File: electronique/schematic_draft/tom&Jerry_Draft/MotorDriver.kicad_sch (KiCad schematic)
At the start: 9 parts, among them IC1401 NCS199A2RSQT2G, U1401 ZXBM5210-S

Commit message: STM32 KiCAD V5 - 20.09.2024
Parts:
- added D1401, D1402: RED, LED_SMD:LED_0603_1608Metric_Pad1.05x0.95mm_HandSolder, symbol Device:LED_Small
- added R1403, R1404: 390R, Resistor_SMD:R_0603_1608Metric_Pad0.98x0.95mm_HandSolder, symbol Device:R_Small
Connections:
- net GND: now also R1403.2, R1404.2
- net PWM_MOTx_CH1: now also D1401.2 (A)
- net PWM_MOTx_CH2: now also D1402.2 (A)
- new net: D1402.1 (K), R1404.1
- new net: D1401.1 (K), R1403.1
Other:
- note added: "Frequence du PWM de 10kHZ, pas sure que les LEDS tiennent la frequence"

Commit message: STM32 KiCAD V5 - 25.09.2024 - Ajout connecteurs TOF, ...
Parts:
- IC1401: footprint Library:SOT65P210X110-6N -> Package_TO_SOT_SMD:SC-70-8
- U1401: footprint Package_SO:SOIC-8-1EP_3.9x4.9mm_P1.27mm_EP2.62x3.51mm_ThermalVias -> Package_SO:Diodes_SO-8EP
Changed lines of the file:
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@@
 			)
 		)
-		(property "Footprint" "Package_SO:SOIC-8-1EP_3.9x4.9mm_P1.27mm_EP2.62x3.51mm_ThermalVias"
+		(property "Footprint" "Package_SO:Diodes_SO-8EP"
 			(at 119.38 107.95 0)
 			(effects
@@
 			)
 		)
-		(property "Footprint" "Library:SOT65P210X110-6N"
+		(property "Footprint" "Package_TO_SOT_SMD:SC-70-8"
 			(at 149.86 -11.1 0)
 			(effects

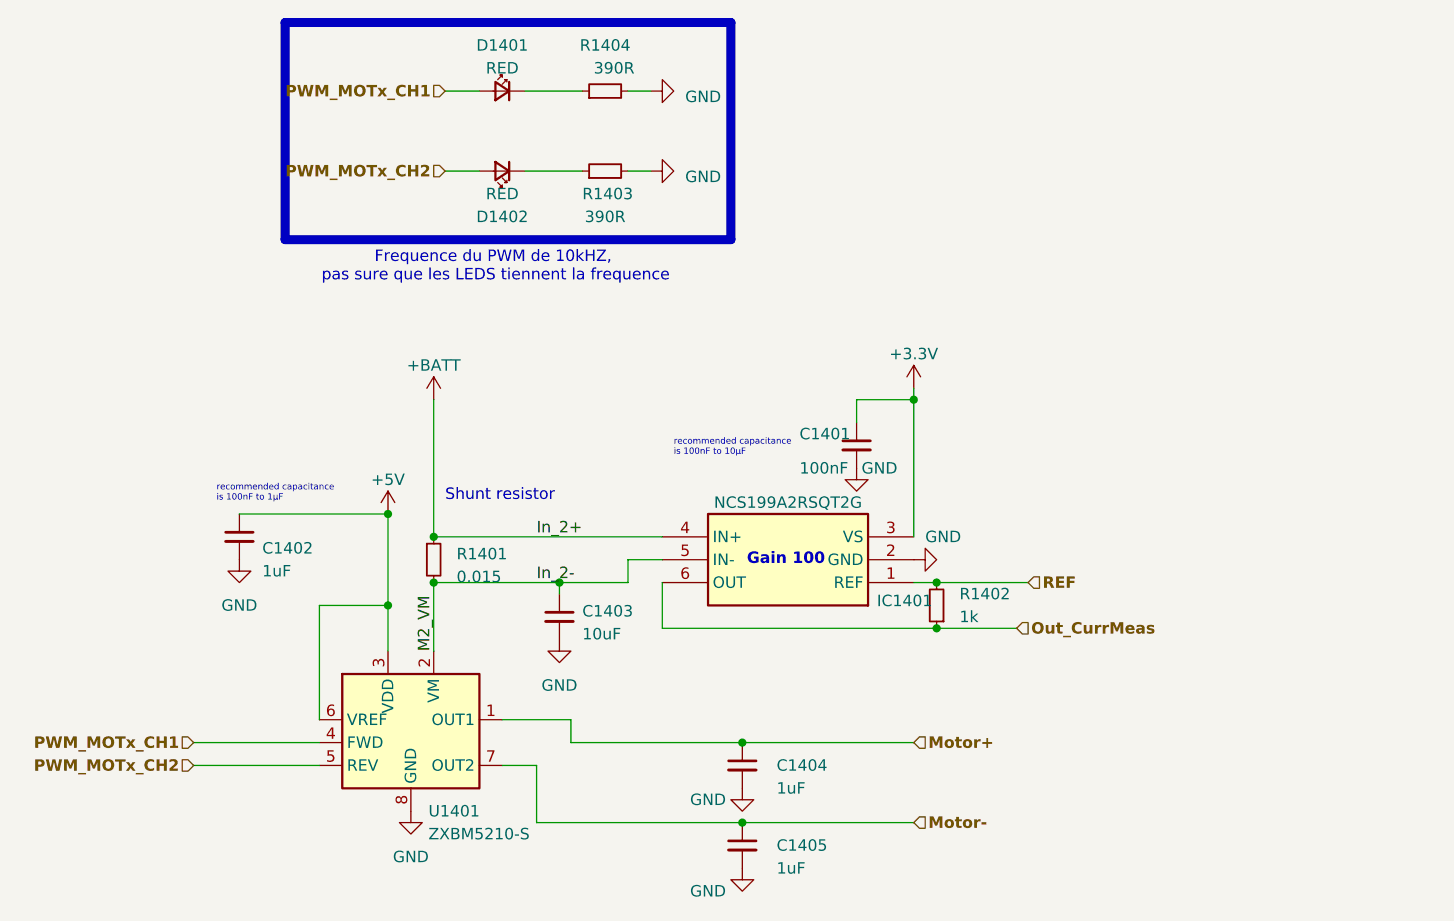
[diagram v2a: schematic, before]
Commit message: STM32 KiCAD v2.0 x CubeIDE - Pin definitif + schematic reviewed
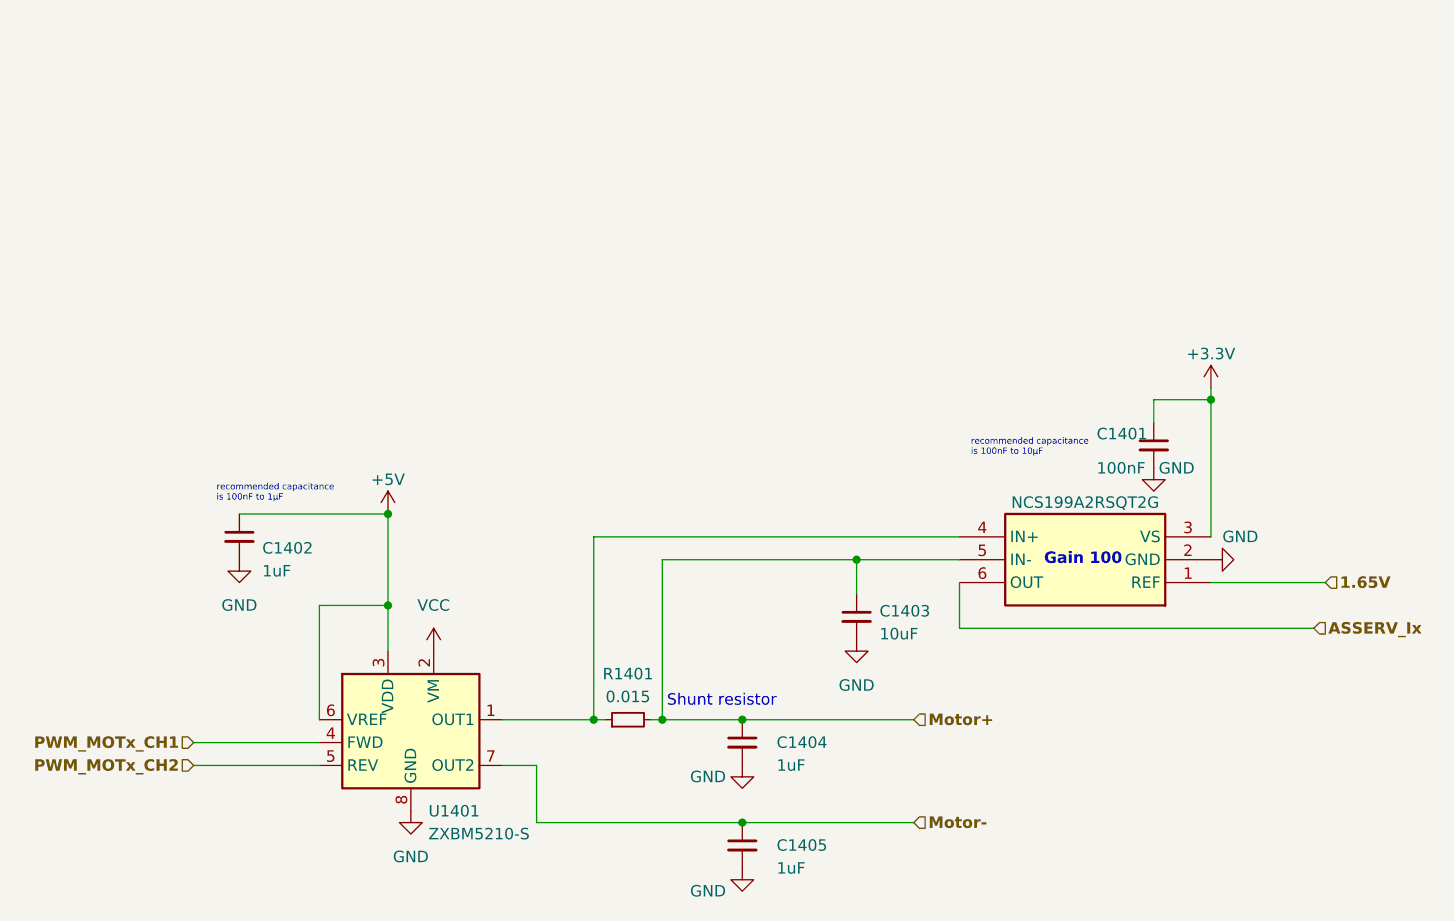
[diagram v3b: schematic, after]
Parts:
- removed D1401, D1402: RED, LED_SMD:LED_0603_1608Metric_Pad1.05x0.95mm_HandSolder, symbol Device:LED_Small
- removed R1402: 1k, symbol Device:R_Small
- removed R1403, R1404: 390R, Resistor_SMD:R_0603_1608Metric_Pad0.98x0.95mm_HandSolder, symbol Device:R_Small
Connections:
- net Motor+: now also C1403.1, IC1401.5 (IN-), R1401.2; no longer U1401.1 (OUT1)
- net +BATT: no longer names the net of IC1401.4 (IN+), R1401.1
- net +BATT: now also U1401.1 (OUT1)
- removed net In_2-: C1403.1, IC1401.5 (IN-), R1401.2, U1401.2 (VM)
- net Out_CurrMeas renamed ASSERV_Ix
- net REF renamed 1.65V
- new net VCC: U1401.2 (VM)
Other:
- note removed: "Frequence du PWM de 10kHZ, pas sure que les LEDS tiennent la frequence"
- moved on the sheet: C1401, C1403, C1404

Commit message: Adding footprint V0.1
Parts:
- C1401: footprint Capacitor_SMD:C_0603_1608Metric_Pad1.08x0.95mm_HandSolder -> Capacitor_SMD:C_0402_1005Metric
- C1402, C1403, C1404, C1405: footprint Capacitor_SMD:C_0603_1608Metric_Pad1.08x0.95mm_HandSolder -> Capacitor_SMD:C_0603_1608Metric
- IC1401: footprint Package_TO_SOT_SMD:SC-70-8 -> Tom&Jerry:SOT65P210X110-6N
- R1401: footprint Resistor_SMD:R_1206_3216Metric_Pad1.30x1.75mm_HandSolder -> Resistor_SMD:R_0402_1005Metric
- U1401: footprint Package_SO:Diodes_SO-8EP -> Tom&Jerry:SOIC127P600X175-8N
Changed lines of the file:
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@@
 			)
 		)
-		(property "Footprint" "Capacitor_SMD:C_0603_1608Metric_Pad1.08x0.95mm_HandSolder"
+		(property "Footprint" "Capacitor_SMD:C_0603_1608Metric"
 			(at 154.94 113.03 0)
 			(effects
@@
 			)
 		)
-		(property "Footprint" "Capacitor_SMD:C_0603_1608Metric_Pad1.08x0.95mm_HandSolder"
+		(property "Footprint" "Capacitor_SMD:C_0603_1608Metric"
 			(at 167.64 87.63 0)
 			(effects
@@
 			)
 		)
-		(property "Footprint" "Package_SO:Diodes_SO-8EP"
+		(property "Footprint" "Tom&Jerry:SOIC127P600X175-8N"
 			(at 119.38 107.95 0)
 			(effects
@@
 			)
 		)
-		(property "Footprint" "Resistor_SMD:R_1206_3216Metric_Pad1.30x1.75mm_HandSolder"
+		(property "Footprint" "Resistor_SMD:R_0402_1005Metric"
 			(at 142.24 99.06 0)
 			(effects
@@
 			)
 		)
-		(property "Footprint" "Capacitor_SMD:C_0603_1608Metric_Pad1.08x0.95mm_HandSolder"
+		(property "Footprint" "Capacitor_SMD:C_0603_1608Metric"
 			(at 99.06 78.74 0)
 			(effects
@@
 			)
 		)
-		(property "Footprint" "Capacitor_SMD:C_0603_1608Metric_Pad1.08x0.95mm_HandSolder"
+		(property "Footprint" "Capacitor_SMD:C_0603_1608Metric"
 			(at 154.94 101.6 0)
 			(effects
@@
 			)
 		)
-		(property "Footprint" "Package_TO_SOT_SMD:SC-70-8"
+		(property "Footprint" "Tom&Jerry:SOT65P210X110-6N"
 			(at 182.88 -11.1 0)
 			(effects
@@
 			)
 		)
-		(property "Footprint" "Capacitor_SMD:C_0603_1608Metric_Pad1.08x0.95mm_HandSolder"
+		(property "Footprint" "Capacitor_SMD:C_0402_1005Metric"
 			(at 200.66 68.58 0)
 			(effects

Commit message: Ajout des bonnes empreintes
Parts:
- U1401: footprint Tom&Jerry:SOIC127P600X175-8N -> Tom&Jerry:XBM5210
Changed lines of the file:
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@@
 			)
 		)
-		(property "Footprint" "Tom&Jerry:SOIC127P600X175-8N"
+		(property "Footprint" "Tom&Jerry:XBM5210"
 			(at 119.38 107.95 0)
 			(effects

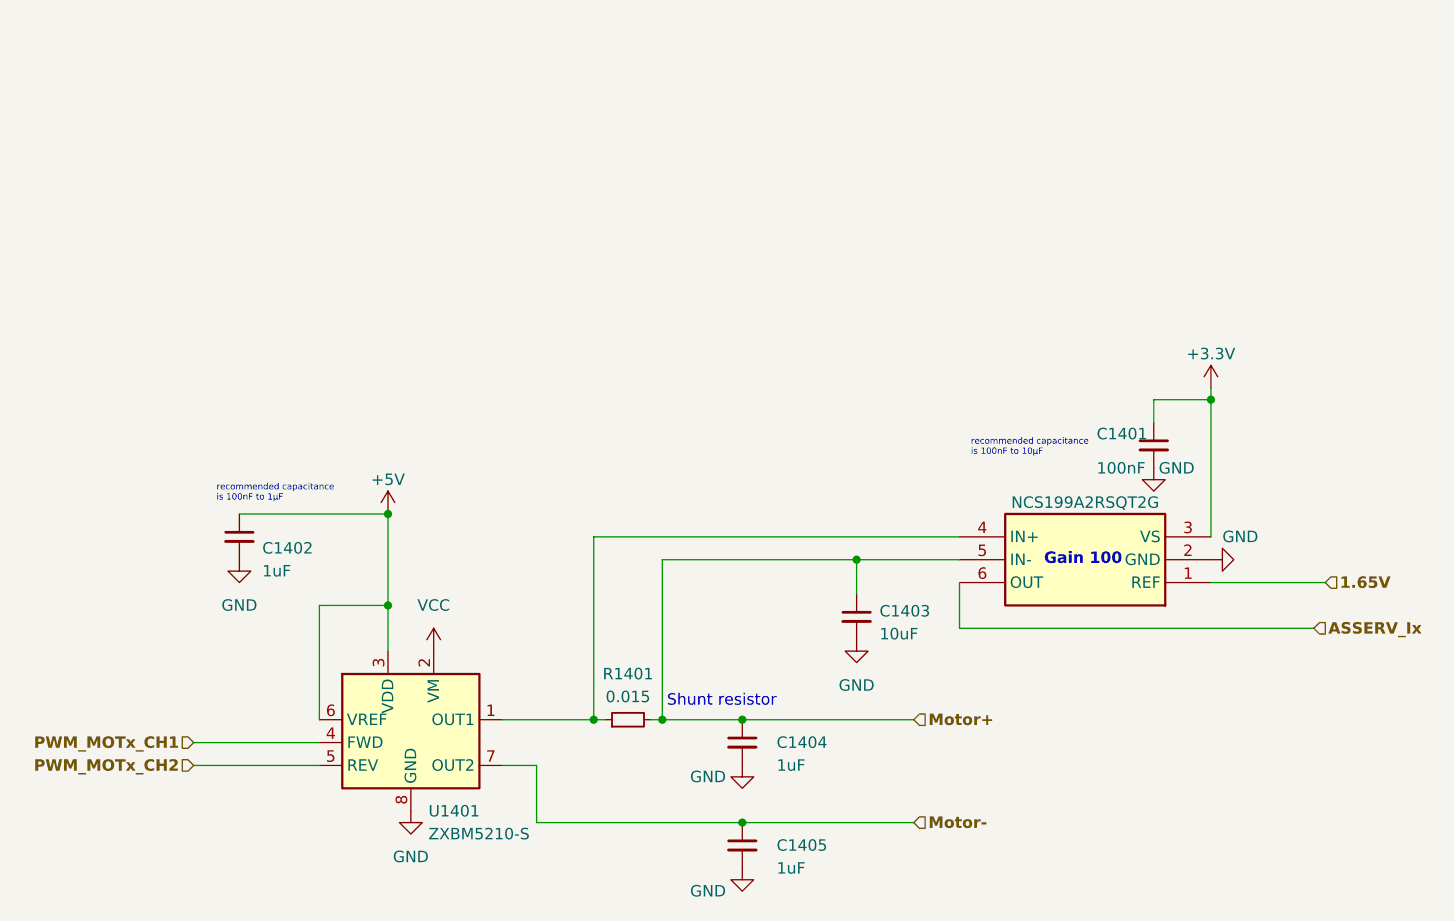
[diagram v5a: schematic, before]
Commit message: Ajout V2 TOF + MultiPCB Panalize
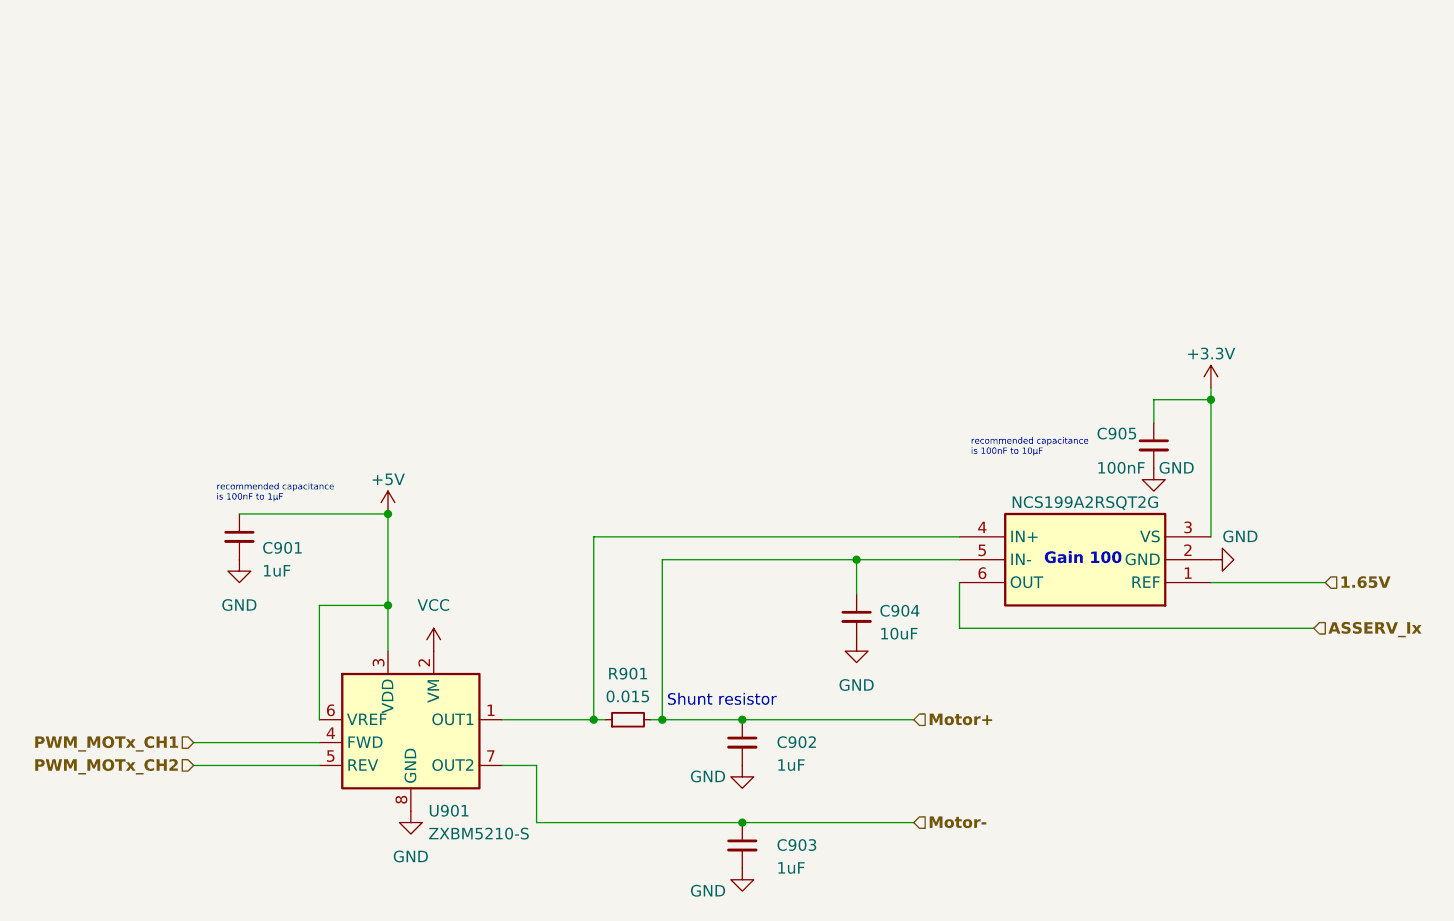
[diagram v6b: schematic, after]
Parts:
- renumbered C1402 to C901, C1404 to C902, C1405 to C903, C1403 to C904, C1401 to C905, IC1401 to IC901, R1401 to R901, U1401 to U901

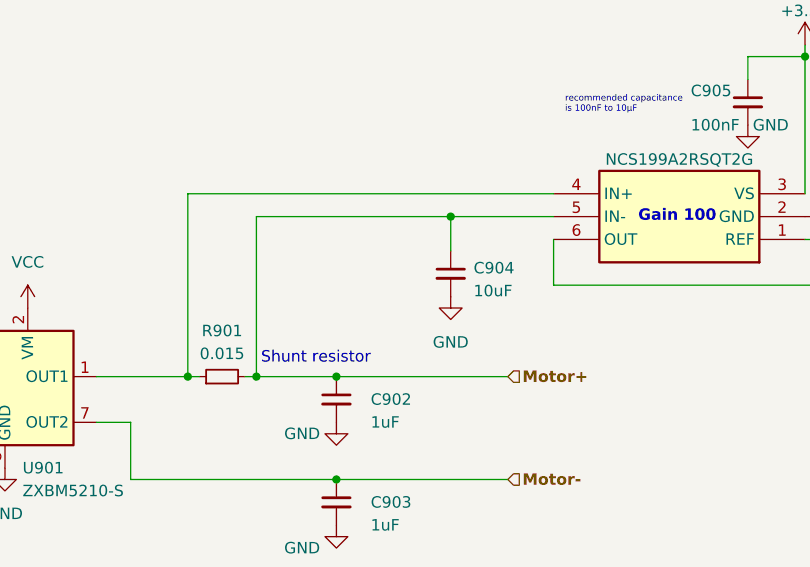
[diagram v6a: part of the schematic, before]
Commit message: V2.0 placement avec tout dessus
Aucun routage réalisé
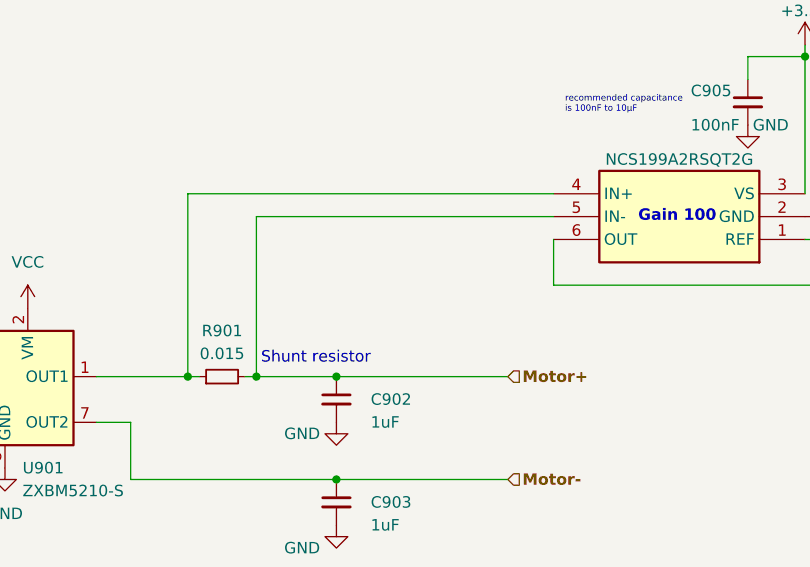
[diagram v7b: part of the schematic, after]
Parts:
- removed C904: 10uF, Capacitor_SMD:C_0603_1608Metric, symbol Device:C_Small
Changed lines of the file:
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@@
-	)
-	(junction
-		(at 167.64 81.28)
-		(diameter 0)
-		(color 0 0 0 0)
 	)
 	(junction
@@
 	(wire
 		(pts
-			(xy 167.64 81.28) (xy 167.64 85.09)
-		)
-		(stroke
-			(width 0)
-			(type default)
-		)
-	)
-	(wire
-		(pts
 			(xy 128.27 99.06) (xy 138.43 99.06)
 		)
@@
 	(wire
 		(pts
-			(xy 167.64 81.28) (xy 179.07 81.28)
-		)
-		(stroke
-			(width 0)
-			(type default)
-		)
-	)
-	(wire
-		(pts
-			(xy 167.64 81.28) (xy 146.05 81.28)
+			(xy 146.05 81.28) (xy 179.07 81.28)
 		)
 		(stroke
@@
 			)
 			(justify right)
-		)
-	)
-	(symbol
-		(lib_id "power:GND")
-		(at 167.64 90.17 0)
-		(unit 1)
-		(exclude_from_sim no)
-		(in_bom yes)
-		(on_board yes)
-		(dnp no)
-		(fields_autoplaced yes)
-		(property "Reference" "#PWR0907"
-			(at 167.64 96.52 0)
-			(effects
-				(font
-					(size 1.27 1.27)
-				)
-				(hide yes)
-			)
-		)
-		(property "Value" "GND"
-			(at 167.64 95.25 0)
-			(effects
-				(font
-					(size 1.27 1.27)
-				)
-			)
-		)
-		(property "Footprint" ""
-			(at 167.64 90.17 0)
-			(effects
-				(font
-					(size 1.27 1.27)
-				)
-				(hide yes)
-			)
-		)
-		(property "Datasheet" ""
-			(at 167.64 90.17 0)
-			(effects
-				(font
-					(size 1.27 1.27)
-				)
-				(hide yes)
-			)
-		)
-		(property "Description" ""
-			(at 167.64 90.17 0)
-			(effects
-				(font
-					(size 1.27 1.27)
-				)
-				(hide yes)
-			)
-		)
-		(pin "1"
-		)
-		(instances
-			(project "tom&Jerry_Draft"
-				(path "/d6e3fbeb-d028-494d-83bf-2e4a8b12578d/13841eaf-0cae-41af-843d-366bf7922a88/0f450893-0917-4549-b275-81de1731d970"
-					(reference "#PWR0907")
-					(unit 1)
-				)
-				(path "/d6e3fbeb-d028-494d-83bf-2e4a8b12578d/13841eaf-0cae-41af-843d-366bf7922a88/e8ed1c1f-b4de-452e-87ed-c5746bc5ffa3"
-					(reference "#PWR01007")
-					(unit 1)
-				)
-			)
 		)
 	)
@@
 					(unit 1)
 				)
-			)
-		)
-	)
-	(symbol
-		(lib_id "Device:C_Small")
-		(at 167.64 87.63 0)
-		(unit 1)
-		(exclude_from_sim no)
-		(in_bom yes)
-		(on_board yes)
-		(dnp no)
-		(fields_autoplaced yes)
-		(property "Reference" "C904"
-			(at 170.18 87.0013 0)
-			(effects
-				(font
-					(size 1.27 1.27)
-				)
-				(justify left)
-			)
-		)
-		(property "Value" "10uF"
-			(at 170.18 89.5413 0)
-			(effects
-				(font
-					(size 1.27 1.27)
-				)
-				(justify left)
-			)
-		)
-		(property "Footprint" "Capacitor_SMD:C_0603_1608Metric"
-			(at 167.64 87.63 0)
-			(effects
-				(font
-					(size 1.27 1.27)
-				)
-				(hide yes)
-			)
-		)
-		(property "Datasheet" "~"
-			(at 167.64 87.63 0)
-			(effects
-				(font
-					(size 1.27 1.27)
-				)
-				(hide yes)
-			)
-		)
-		(property "Description" ""
-			(at 167.64 87.63 0)
-			(effects
-				(font
-					(size 1.27 1.27)
-				)
-				(hide yes)
-			)
-		)
-		(pin "1"
-		)
-		(pin "2"
-		)
-		(instances
-			(project "tom&Jerry_Draft"
-				(path "/d6e3fbeb-d028-494d-83bf-2e4a8b12578d/13841eaf-0cae-41af-843d-366bf7922a88/0f450893-0917-4549-b275-81de1731d970"
-					(reference "C904")
-					(unit 1)
-				)
-				(path "/d6e3fbeb-d028-494d-83bf-2e4a8b12578d/13841eaf-0cae-41af-843d-366bf7922a88/e8ed1c1f-b4de-452e-87ed-c5746bc5ffa3"
-					(reference "C1004")
-					(unit 1)
-				)

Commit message: Routage Signal Complet - PCB V2.0
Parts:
- renumbered C905 to C901, C901 to C902, C902 to C903, C903 to C904
